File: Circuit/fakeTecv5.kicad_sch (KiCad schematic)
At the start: 76 parts, among them J1 EXTRA, J11 FET1 3,3, J12 FET2 3,3, J13 FET3 3,3, J14 GPS Pins, J16 Encoder Pads, J37 SCL, J38 JST-SH-4, J39 SDA, J40 3.3V, J41 GND, J42 FET1, J43 FET2, J44 FET3, J45 GND, J46 3.3V, J47 GND, J48 GND, J49 GND, J5 I2C Oled screen, J50 3.3V, J51 GND, J52 GND, J6 FET1 Drain, J7 FET2 Drain, J8 FET3 Drain, J9 JST-PH-2, M1 ERM Motor, Q1 AO3400A, Q2 AO3400A, Q3 AO3400A, SW1 Reset, SW2 SW_Push, SW3 RotaryEncoder_Switch, U1 XB8089D0, U2 HT-RA62, U3 nice!nano v2

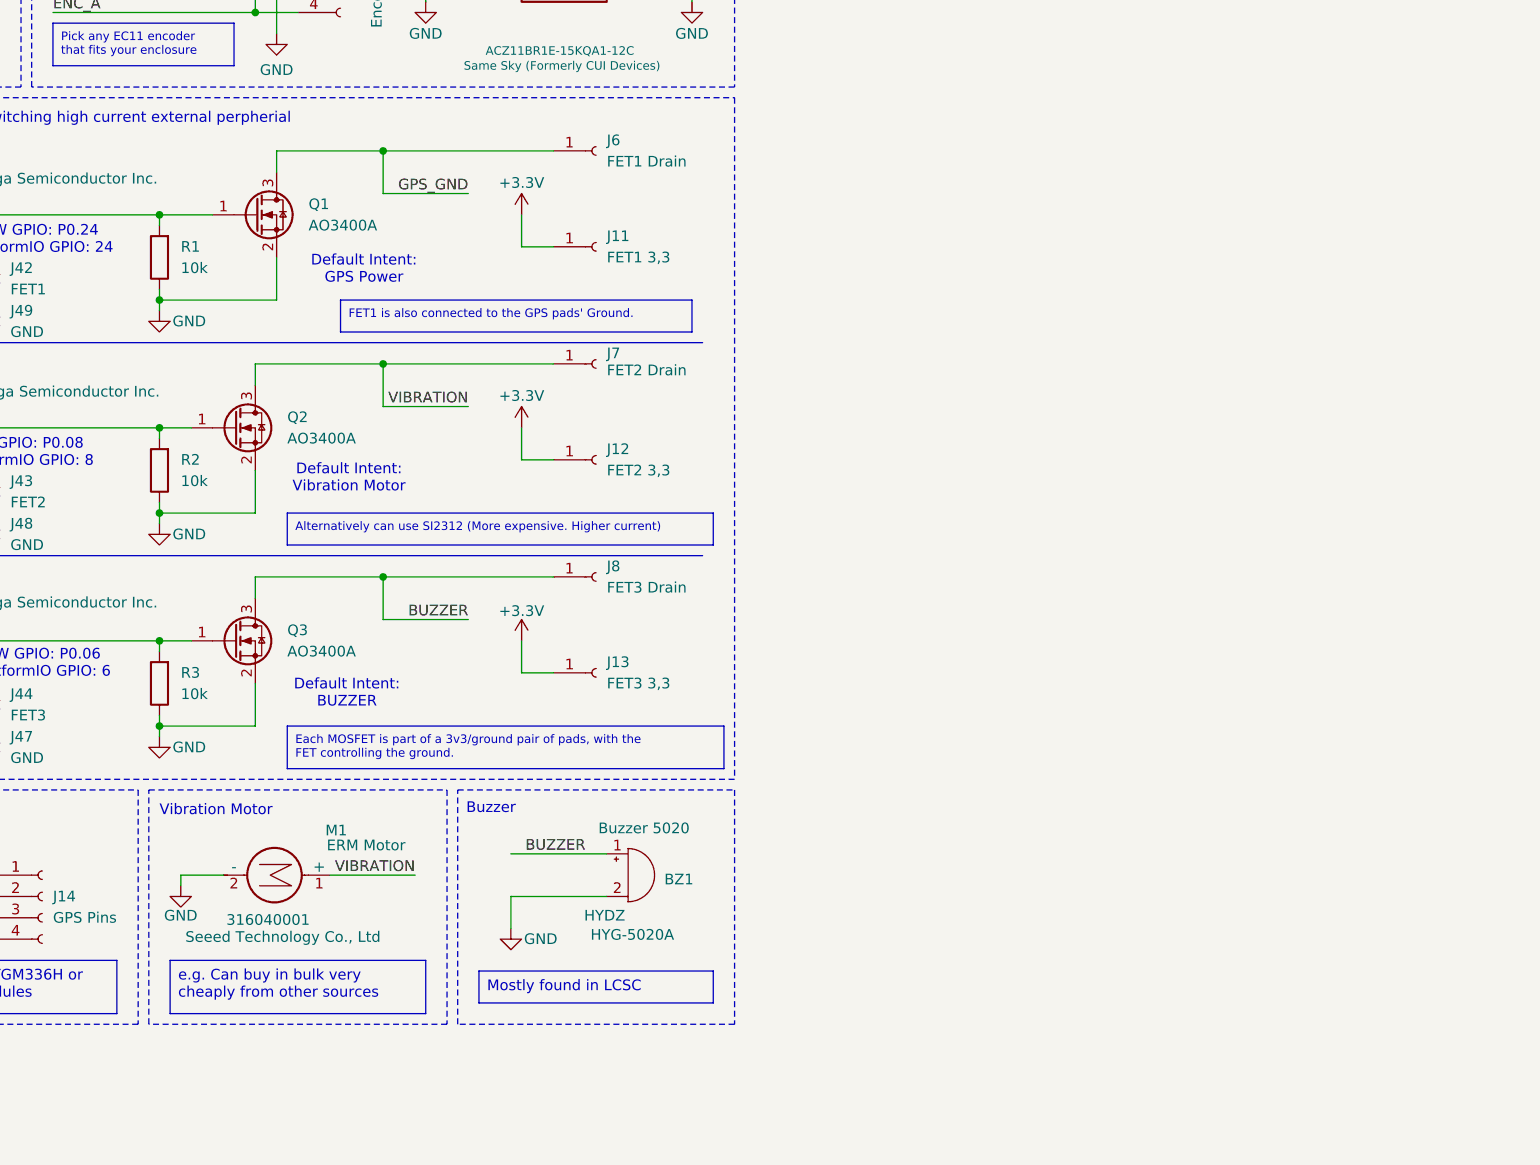
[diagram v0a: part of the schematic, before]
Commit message: hw: Buzzer is wired incorrectly. Fixed wiring and updated schematic and pcb
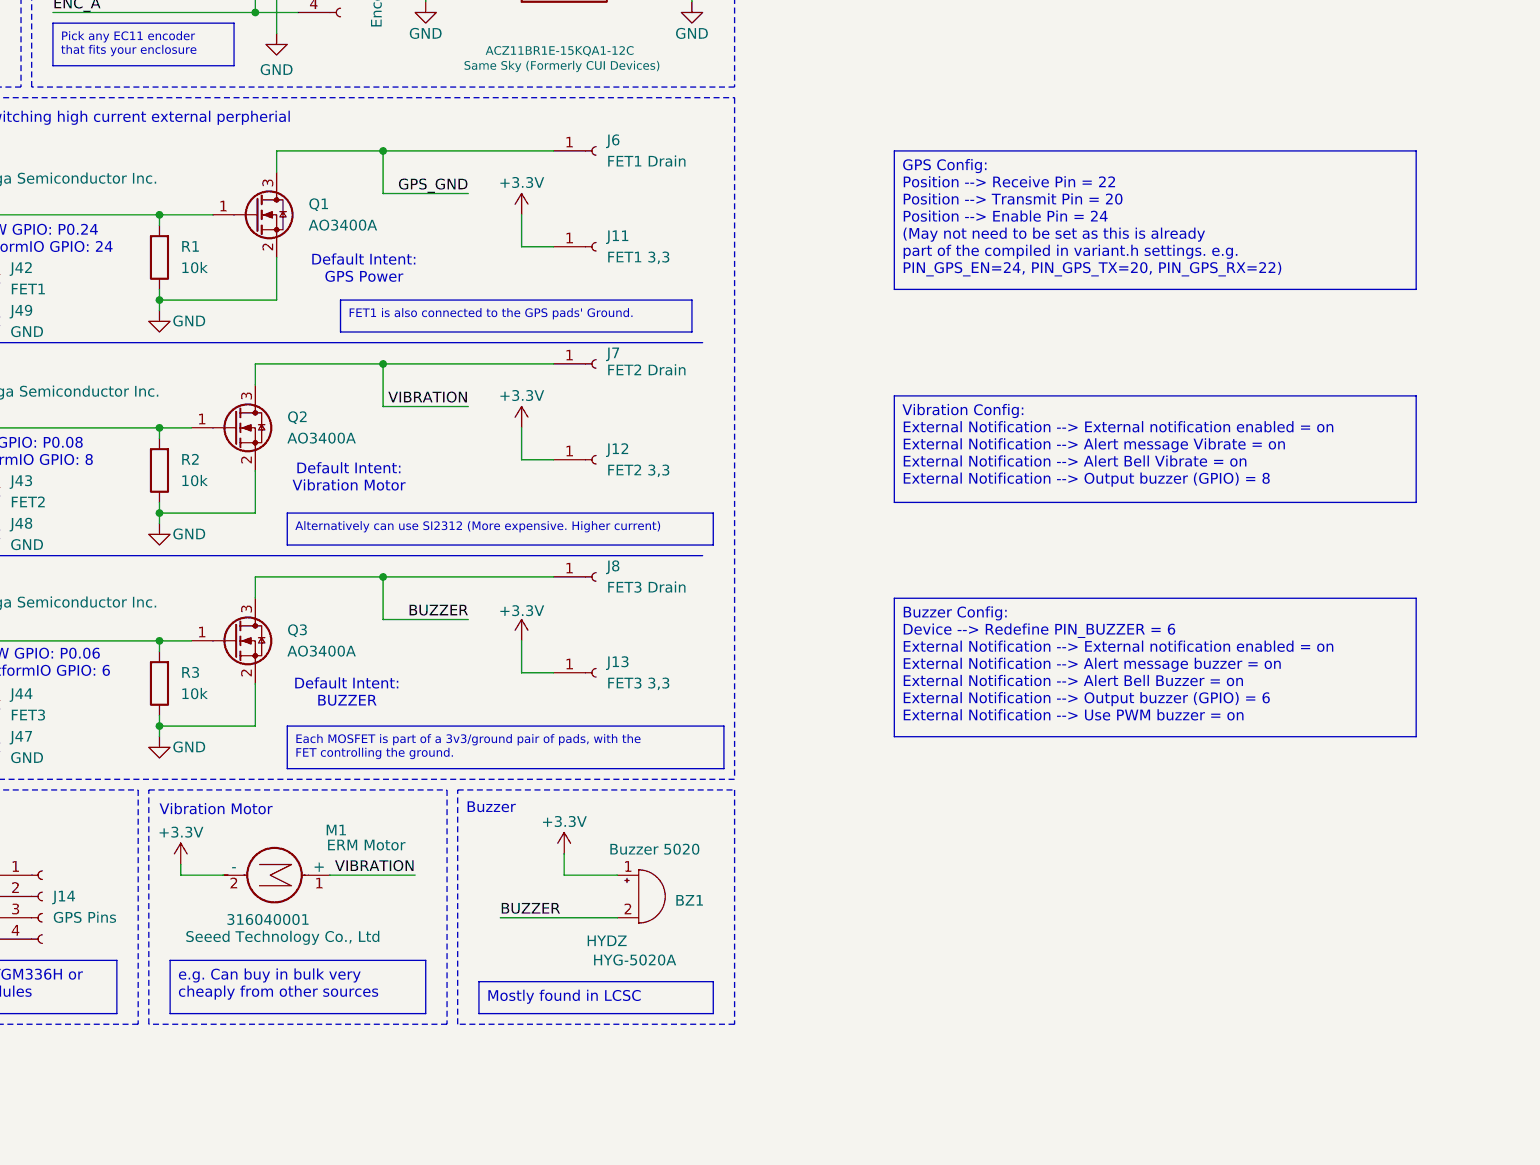
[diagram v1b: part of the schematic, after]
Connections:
- net +3.3V: now also BZ1.1 (+), M1.2 (-)
- net BUZZER: now also BZ1.2 (-); no longer BZ1.1 (+)
- net GND: no longer BZ1.2 (-), M1.2 (-)
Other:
- moved on the sheet: BZ1

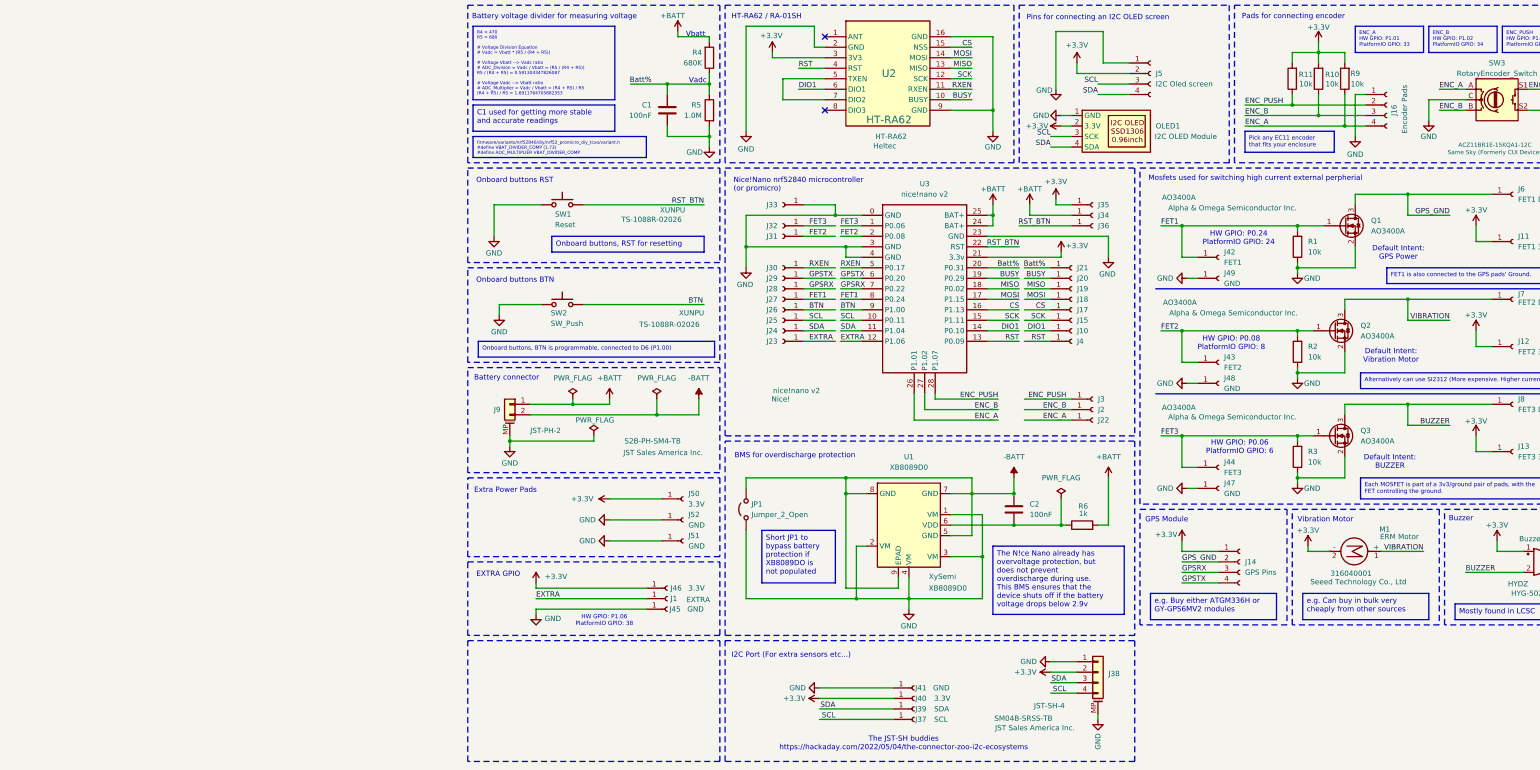
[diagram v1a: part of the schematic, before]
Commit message: hw: Battery connector clarification
Heltec LoRa32 is using Molex Picoblade... not JST
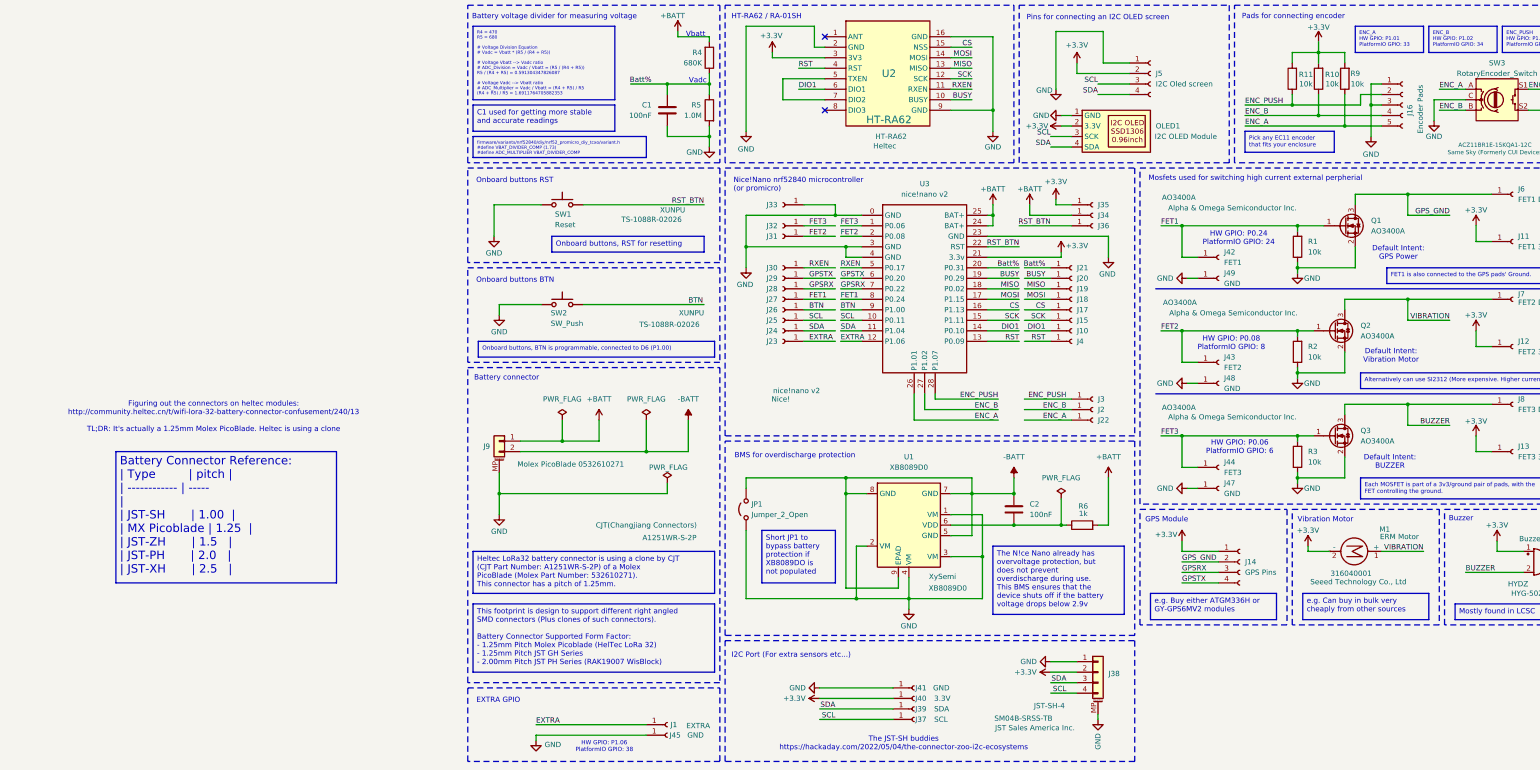
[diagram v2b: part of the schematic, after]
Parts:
- removed J46, J50: 3.3V, faketec:SMD_PAD_1x01, symbol Connector:Conn_01x01_Socket
- removed J51, J52: GND, faketec:SMD_PAD_1x01, symbol Connector:Conn_01x01_Socket
- J16: footprint faketec:SMD_PAD_1x04 -> faketec:SMD_PAD_1x05; symbol Connector:Conn_01x04_Socket -> Connector:Conn_01x05_Socket; now in the parts list
- J9: value JST-PH-2 -> Molex PicoBlade 0532610271; MPD 2P 1x2P PH Tin -25℃~+85℃ Beige 2mm 100V 2 2A 1 Surface Moun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 -> Connector Header 2 position 1.25mm Pitch; MPL https://www.lcsc.com/product-detail/C295747.html?s_z=n_S2B-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 -> https://www.lcsc.com/product-detail/C225111.html; MPN S2B-PH-SM4-TB -> A1251WR-S-2P; Manufacturer JST Sales America Inc. -> CJT(Changjiang Connectors); Package SMD,P=2mm,Surface Mount,Right Angle -> SMD,P=1.25mm,Surface Mount,Right Angle; Shopping https://www.lcsc.com/search?q=S2B-PH-SM4-TB&s_z=n_S2B-PH-SM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 -> https://www.lcsc.com/search?q=0532610271&s_z=n_0532610271
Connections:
- net ENC_A: now also J16.5 (Pin_5); no longer J16.4 (Pin_4)
- net ENC_B: now also J16.4 (Pin_4); no longer J16.3 (Pin_3)
- net GND: now also J16.3 (Pin_3)
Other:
- note added: "Figuring out the connectors on heltec modules: http://community.heltec.cn/t/wifi-lora-32-battery-connector-confusement/240/13 TL;DR: It's actually a 1.25mm Molex PicoBlade. Heltec is using a clone"
- note removed: "Extra Power Pads"
- moved on the sheet: J1, J45, J9
